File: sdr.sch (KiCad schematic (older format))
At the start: 3 parts

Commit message: RF filter implemented
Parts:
- U?: symbol RF_Mixer:ADE-6 -> sdr-rescue:ADE-6-RF_Mixer
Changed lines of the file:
@@
 S 1500 3350 750  250
 U 5FE31D05
-F0 "Sheet5FE31D04" 50
+F0 "30MHz LPF" 50
 F1 "rf_lpf.sch" 50
 F2 "IN" I L 1500 3450 50
-F3 "OUT" I R 2250 3450 50
+F3 "OUT" O R 2250 3450 50
 $EndSheet
 $Sheet
@@
 $EndSheet
 $Comp
-L RF_Mixer:ADE-6 U?
+L sdr-rescue:ADE-6-RF_Mixer U?
 U 1 1 5FE32B05
 P 4100 3450

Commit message: Attenuator revised
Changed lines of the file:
@@
 F3 "OUT" O R 2250 3450 50
-$EndSheet
-$Sheet
-S 2600 3350 900  250
-U 5FE31E1E
-F0 "Sheet5FE31E1D" 50
-F1 "rf_autt.sch" 50
 $EndSheet
 $Comp
@@
 	1    0    0    -1
 $EndComp
+$Sheet
+S 2600 3350 900  600
+U 5FE31E1E
+F0 "Attenuator" 50
+F1 "rf_autt.sch" 50
+F2 "IN" I L 2600 3450 50
+F3 "OUT" O R 3500 3450 50
+F4 "ATT_SEL0" I L 2600 3750 50
+F5 "ATT_SEL1" I L 2600 3850 50
+$EndSheet
+Wire Wire Line
+	2250 3450 2600 3450
 $EndSCHEMATC

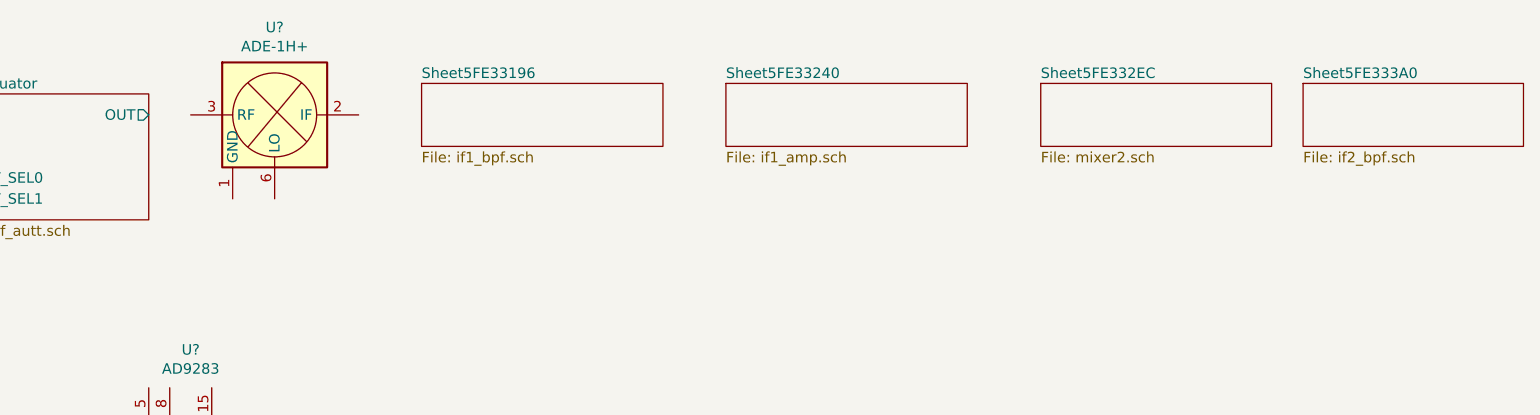
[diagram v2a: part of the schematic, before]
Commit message: Second mixer
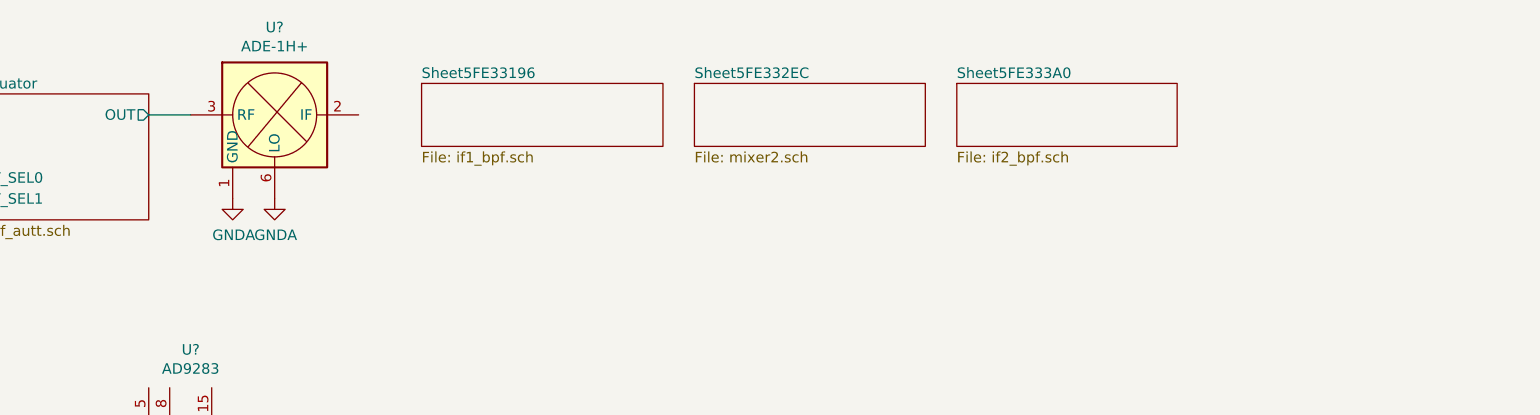
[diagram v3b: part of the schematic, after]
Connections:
- net Attenuator/OUT: now also U?.3 (RF)
- net GNDA: now also U?.1 (GND), U?.4 (GND), U?.5 (GND), U?.6 (LO)
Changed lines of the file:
@@
 $Descr A4 11693 8268
 encoding utf-8
-Sheet 1 8
+Sheet 1 7
 Title ""
 Date ""
@@
 $EndSheet
 $Sheet
-S 6250 3300 1150 300
-U 5FE33241
-F0 "Sheet5FE33240" 50
-F1 "if1_amp.sch" 50
-$EndSheet
-$Sheet
-S 7750 3300 1100 300
+S 6100 3300 1100 300
 U 5FE332ED
 F0 "Sheet5FE332EC" 50
@@
 $EndSheet
 $Sheet
-S 9000 3300 1050 300
+S 7350 3300 1050 300
 U 5FE333A1
 F0 "Sheet5FE333A0" 50
@@
 Wire Wire Line
 	2250 3450 2600 3450
+Wire Wire Line
+	3500 3450 3700 3450
+$Comp
+L power:GNDA #PWR?
+U 1 1 5FE67095
+P 3900 3850
+F 0 "#PWR?" H 3900 3600 50  0001 C CNN
+F 1 "GNDA" H 3905 3677 50  0000 C CNN
+F 2 "" H 3900 3850 50  0001 C CNN
+F 3 "" H 3900 3850 50  0001 C CNN
+	1    3900 3850
+	1    0    0    -1
+$EndComp
+$Comp
+L power:GNDA #PWR?
+U 1 1 5FE6714C
+P 4100 3850
+F 0 "#PWR?" H 4100 3600 50  0001 C CNN
+F 1 "GNDA" H 4105 3677 50  0000 C CNN
+F 2 "" H 4100 3850 50  0001 C CNN
+F 3 "" H 4100 3850 50  0001 C CNN
+	1    4100 3850
+	1    0    0    -1
+$EndComp
 $EndSCHEMATC

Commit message: 37.4Mega
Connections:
- net 37.4 MHz Butterworth BPF/IN: now reaches U?.2 (IF)
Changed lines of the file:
@@
 S 4800 3300 1150 300
 U 5FE33197
-F0 "Sheet5FE33196" 50
+F0 "37.4 MHz Butterworth BPF" 50
 F1 "if1_bpf.sch" 50
+F2 "IN" I L 4800 3450 50
+F3 "OUT" I R 5950 3450 50
 $EndSheet
 $Sheet
@@
 	1    0    0    -1
 $EndComp
+Wire Wire Line
+	4800 3450 4500 3450
 $EndSCHEMATC

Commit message: Block diagram arrangement
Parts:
- added K? (x3): FRT5_separated, Relay_THT:Relay_DPDT_FRT5, symbol Relay:FRT5_separated
- added R?: 0 DNP, symbol Device:R
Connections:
- wire segments 4 -> 23
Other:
- note added: "Switchable bga2866??"
- moved on the sheet: J?, U?
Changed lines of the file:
@@
 L Connector:Conn_Coaxial J?
 U 1 1 5FE31A99
-P 850 3450
-F 0 "J?" H 778 3688 50  0000 C CNN
-F 1 "Conn_Coaxial" H 778 3597 50  0000 C CNN
-F 2 "" H 850 3450 50  0001 C CNN
-F 3 " ~" H 850 3450 50  0001 C CNN
-	1    850  3450
+P 850 3650
+F 0 "J?" H 778 3888 50  0000 C CNN
+F 1 "Conn_Coaxial" H 778 3797 50  0000 C CNN
+F 2 "" H 850 3650 50  0001 C CNN
+F 3 " ~" H 850 3650 50  0001 C CNN
+	1    850  3650
 	-1   0    0    -1
 $EndComp
 $Sheet
-S 1500 3350 750  250
+S 1150 1250 750  250
 U 5FE31D05
 F0 "30MHz LPF" 50
 F1 "rf_lpf.sch" 50
-F2 "IN" I L 1500 3450 50
-F3 "OUT" O R 2250 3450 50
+F2 "IN" I L 1150 1350 50
+F3 "OUT" O R 1900 1350 50
 $EndSheet
 $Comp
 L sdr-rescue:ADE-6-RF_Mixer U?
 U 1 1 5FE32B05
-P 4100 3450
-F 0 "U?" H 4100 3867 50  0000 C CNN
-F 1 "ADE-1H+" H 4100 3776 50  0000 C CNN
-F 2 "RF_Mini-Circuits:Mini-Circuits_CD542_LandPatternPL-052" H 4175 3075 50  0001 C CNN
-F 3 "https://www.minicircuits.com/pdfs/ADE-6.pdf" H 4275 3175 50  0001 C CNN
-	1    4100 3450
+P 3300 1350
+F 0 "U?" H 3300 1767 50  0000 C CNN
+F 1 "ADE-1H+" H 3300 1676 50  0000 C CNN
+F 2 "RF_Mini-Circuits:Mini-Circuits_CD542_LandPatternPL-052" H 3375 975 50  0001 C CNN
+F 3 "https://www.minicircuits.com/pdfs/ADE-6.pdf" H 3475 1075 50  0001 C CNN
+	1    3300 1350
 	1    0    0    -1
 $EndComp
 $Sheet
-S 4800 3300 1150 300
+S 3750 1200 1250 300
 U 5FE33197
 F0 "37.4 MHz Butterworth BPF" 50
 F1 "if1_bpf.sch" 50
-F2 "IN" I L 4800 3450 50
-F3 "OUT" I R 5950 3450 50
+F2 "IN" I L 3750 1350 50
+F3 "OUT" I R 5000 1350 50
 $EndSheet
 $Sheet
-S 6100 3300 1100 300
+S 5100 1200 1450 300
 U 5FE332ED
-F0 "Sheet5FE332EC" 50
+F0 "37.4 MHz Amp, and 2nd mixer" 50
 F1 "mixer2.sch" 50
+F2 "out_p" I R 6550 1300 50
+F3 "out_n" I R 6550 1400 50
+F4 "IN" I L 5100 1350 50
 $EndSheet
 $Sheet
-S 7350 3300 1050 300
+S 6700 1200 1050 300
 U 5FE333A1
 F0 "Sheet5FE333A0" 50
@@
 $EndSheet
 $Sheet
-S 750  5050 1300 350
+S 7850 1200 1300 350
 U 5FE3342F
 F0 "Sheet5FE3342E" 50
@@
 L Analog_ADC:AD9283 U?
 U 1 1 5FE337CA
-P 3700 5550
-F 0 "U?" H 3700 6531 50  0000 C CNN
-F 1 "AD9283" H 3700 6440 50  0000 C CNN
-F 2 "" H 3700 5550 50  0001 C CNN
-F 3 "https://www.analog.com/media/en/technical-documentation/data-sheets/AD9283.pdf" H 3700 5550 50  0001 C CNN
-	1    3700 5550
-	1    0    0    -1
-$EndComp
-Wire Wire Line
-	1500 3450 1050 3450
-$Comp
-L power:GNDA #PWR?
-U 1 1 5FE34F57
-P 850 3650
-F 0 "#PWR?" H 850 3400 50  0001 C CNN
-F 1 "GNDA" H 855 3477 50  0000 C CNN
-F 2 "" H 850 3650 50  0001 C CNN
-F 3 "" H 850 3650 50  0001 C CNN
-	1    850  3650
-	1    0    0    -1
-$EndComp
-$Sheet
-S 2600 3350 900  600
-U 5FE31E1E
-F0 "Attenuator" 50
-F1 "rf_autt.sch" 50
-F2 "IN" I L 2600 3450 50
-F3 "OUT" O R 3500 3450 50
-F4 "ATT_SEL0" I L 2600 3750 50
-F5 "ATT_SEL1" I L 2600 3850 50
-$EndSheet
-Wire Wire Line
-	2250 3450 2600 3450
-Wire Wire Line
-	3500 3450 3700 3450
-$Comp
-L power:GNDA #PWR?
-U 1 1 5FE67095
-P 3900 3850
-F 0 "#PWR?" H 3900 3600 50  0001 C CNN
-F 1 "GNDA" H 3905 3677 50  0000 C CNN
-F 2 "" H 3900 3850 50  0001 C CNN
-F 3 "" H 3900 3850 50  0001 C CNN
-	1    3900 3850
+P 10050 1700
+F 0 "U?" H 10050 2681 50  0000 C CNN
+F 1 "AD9283" H 10050 2590 50  0000 C CNN
+F 2 "" H 10050 1700 50  0001 C CNN
+F 3 "https://www.analog.com/media/en/technical-documentation/data-sheets/AD9283.pdf" H 10050 1700 50  0001 C CNN
+	1    10050 1700
 	1    0    0    -1
 $EndComp
 $Comp
 L power:GNDA #PWR?
-U 1 1 5FE6714C
-P 4100 3850
-F 0 "#PWR?" H 4100 3600 50  0001 C CNN
-F 1 "GNDA" H 4105 3677 50  0000 C CNN
-F 2 "" H 4100 3850 50  0001 C CNN
-F 3 "" H 4100 3850 50  0001 C CNN
-	1    4100 3850
+U 1 1 5FE34F57
+P 850 3850
+F 0 "#PWR?" H 850 3600 50  0001 C CNN
+F 1 "GNDA" H 855 3677 50  0000 C CNN
+F 2 "" H 850 3850 50  0001 C CNN
+F 3 "" H 850 3850 50  0001 C CNN
+	1    850  3850
+	1    0    0    -1
+$EndComp
+$Sheet
+S 2050 1250 700  600
+U 5FE31E1E
+F0 "Attenuator" 50
+F1 "rf_autt.sch" 50
+F2 "IN" I L 2050 1350 50
+F3 "OUT" O R 2750 1350 50
+F4 "ATT_SEL0" I L 2050 1650 50
+F5 "ATT_SEL1" I L 2050 1750 50
+$EndSheet
+Wire Wire Line
+	1900 1350 1950 1350
+$Comp
+L power:GNDA #PWR?
+U 1 1 5FE67095
+P 3100 1750
+F 0 "#PWR?" H 3100 1500 50  0001 C CNN
+F 1 "GNDA" H 3105 1577 50  0000 C CNN
+F 2 "" H 3100 1750 50  0001 C CNN
+F 3 "" H 3100 1750 50  0001 C CNN
+	1    3100 1750
 	1    0    0    -1
 $EndComp
 Wire Wire Line
-	4800 3450 4500 3450
+	3750 1350 3700 1350
+$Comp
+L Device:R R?
+U 1 1 5FE74C58
+P 2450 1000
+F 0 "R?" V 2243 1000 50  0000 C CNN
+F 1 "0 DNP" V 2334 1000 50  0000 C CNN
+F 2 "" V 2380 1000 50  0001 C CNN
+F 3 "~" H 2450 1000 50  0001 C CNN
+	1    2450 1000
+	0    1    1    0
+$EndComp
+Wire Wire Line
+	2850 1350 2850 1000
+Wire Wire Line
+	2850 1000 2600 1000
+Connection ~ 2850 1350
+Wire Wire Line
+	2850 1350 2900 1350
+Wire Wire Line
+	2300 1000 1950 1000
+Wire Wire Line
+	1950 1000 1950 1350
+Connection ~ 1950 1350
+Wire Wire Line
+	1950 1350 2050 1350
+Wire Wire Line
+	2750 1350 2850 1350
+Wire Wire Line
+	5100 1350 5000 1350
+$Comp
+L Relay:FRT5_separated K?
+U 1 1 5FE86F08
+P 1400 6450
+F 0 "K?" H 1555 6496 50  0000 L CNN
+F 1 "FRT5_separated" H 1555 6405 50  0000 L CNN
+F 2 "Relay_THT:Relay_DPDT_FRT5" H 1600 6350 50  0001 L CNN
+F 3 "https://www.elpro.org/de/index.php?controller=attachment&id_attachment=8663" H 1400 6450 50  0001 C CNN
+	1    1400 6450
+	1    0    0    -1
+$EndComp
+$Comp
+L Relay:FRT5_separated K?
+U 2 1 5FE88F75
+P 1500 3650
+F 0 "K?" V 1175 3650 50  0000 C CNN
+F 1 "FRT5_separated" V 1266 3650 50  0000 C CNN
+F 2 "Relay_THT:Relay_DPDT_FRT5" H 1700 3550 50  0001 L CNN
+F 3 "https://www.elpro.org/de/index.php?controller=attachment&id_attachment=8663" H 1500 3650 50  0001 C CNN
+	2    1500 3650
+	0    1    1    0
+$EndComp
+$Comp
+L Relay:FRT5_separated K?
+U 3 1 5FE89BA9
+P 2200 4100
+F 0 "K?" H 2344 4146 50  0000 L CNN
+F 1 "FRT5_separated" H 2344 4055 50  0000 L CNN
+F 2 "Relay_THT:Relay_DPDT_FRT5" H 2400 4000 50  0001 L CNN
+F 3 "https://www.elpro.org/de/index.php?controller=attachment&id_attachment=8663" H 2200 4100 50  0001 C CNN
+	3    2200 4100
+	1    0    0    -1
+$EndComp
+Wire Wire Line
+	1800 3550 1900 3550
+Wire Wire Line
+	1900 3550 1900 2100
+Wire Wire Line
+	1900 2100 800  2100
+Wire Wire Line
+	800  2100 800  1350
+Wire Wire Line
+	800  1350 1150 1350
+Wire Wire Line
+	1200 3650 1050 3650
+Wire Wire Line
+	2100 3800 2100 3750
+Wire Wire Line
+	2100 3750 1800 3750
+Wire Wire Line
+	2300 3800 2300 2100
+Wire Wire Line
+	2300 2100 3300 2100
+Wire Wire Line
+	3300 2100 3300 1750
+Wire Wire Line
+	2200 4400 10750 4400
+Wire Wire Line
+	10750 4400 10750 5100
+Text Notes 6250 1850 0    50   ~ 0
+Switchable bga2866??
 $EndSCHEMATC

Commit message: 2nd IF amp test values
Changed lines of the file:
@@
 Wire Wire Line
 	10750 4400 10750 5100
-Text Notes 6250 1850 0    50   ~ 0
+Text Notes 4650 1800 0    50   ~ 0
 Switchable bga2866??
 $EndSCHEMATC

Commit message: if2_amp.sch
if2_amp almost done
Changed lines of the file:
@@
 F0 "Sheet5FE3342E" 50
 F1 "if2_amp.sch" 50
+F2 "In+" I L 7850 1300 50
+F3 "In-" I L 7850 1450 50
+F4 "Out+" I R 9150 1300 50
+F5 "Out-" I R 9150 1450 50
 $EndSheet
 $Comp

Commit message: if2 completed
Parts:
- added R? (x2): 0 DNP, symbol Device:R
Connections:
- wire segments 23 -> 41
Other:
- moved on the sheet: U?
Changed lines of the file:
@@
 $EndSheet
 $Sheet
-S 6700 1200 1050 300
+S 6700 1200 950  400
 U 5FE333A1
 F0 "Sheet5FE333A0" 50
 F1 "if2_bpf.sch" 50
+F2 "Out+" I R 7650 1300 50
+F3 "Out-" I R 7650 1500 50
+F4 "In+" I L 6700 1300 50
+F5 "In-" I L 6700 1400 50
 $EndSheet
 $Sheet
-S 7850 1200 1300 350
+S 7850 1100 1300 500
 U 5FE3342F
 F0 "Sheet5FE3342E" 50
 F1 "if2_amp.sch" 50
 F2 "In+" I L 7850 1300 50
-F3 "In-" I L 7850 1450 50
+F3 "In-" I L 7850 1500 50
 F4 "Out+" I R 9150 1300 50
-F5 "Out-" I R 9150 1450 50
+F5 "Out-" I R 9150 1500 50
 $EndSheet
 $Comp
 L Analog_ADC:AD9283 U?
 U 1 1 5FE337CA
-P 10050 1700
-F 0 "U?" H 10050 2681 50  0000 C CNN
-F 1 "AD9283" H 10050 2590 50  0000 C CNN
-F 2 "" H 10050 1700 50  0001 C CNN
-F 3 "https://www.analog.com/media/en/technical-documentation/data-sheets/AD9283.pdf" H 10050 1700 50  0001 C CNN
-	1    10050 1700
+P 10100 1700
+F 0 "U?" H 10100 2681 50  0000 C CNN
+F 1 "AD9283" H 10100 2590 50  0000 C CNN
+F 2 "" H 10100 1700 50  0001 C CNN
+F 3 "https://www.analog.com/media/en/technical-documentation/data-sheets/AD9283.pdf" H 10100 1700 50  0001 C CNN
+	1    10100 1700
 	1    0    0    -1
 $EndComp
@@
 Text Notes 4650 1800 0    50   ~ 0
 Switchable bga2866??
+$Comp
+L Device:R R?
+U 1 1 5FEA317B
+P 8500 850
+F 0 "R?" V 8293 850 50  0000 C CNN
+F 1 "0 DNP" V 8384 850 50  0000 C CNN
+F 2 "" V 8430 850 50  0001 C CNN
+F 3 "~" H 8500 850 50  0001 C CNN
+	1    8500 850
+	0    1    1    0
+$EndComp
+$Comp
+L Device:R R?
+U 1 1 5FEA3DAB
+P 8500 2000
+F 0 "R?" V 8293 2000 50  0000 C CNN
+F 1 "0 DNP" V 8384 2000 50  0000 C CNN
+F 2 "" V 8430 2000 50  0001 C CNN
+F 3 "~" H 8500 2000 50  0001 C CNN
+	1    8500 2000
+	0    1    1    0
+$EndComp
+Wire Wire Line
+	7850 1300 7800 1300
+Wire Wire Line
+	7800 1300 7800 850
+Wire Wire Line
+	7800 850  8350 850
+Wire Wire Line
+	8650 850  9300 850
+Wire Wire Line
+	9300 850  9300 1300
+Wire Wire Line
+	9150 1300 9300 1300
+Wire Wire Line
+	9300 1500 9150 1500
+Wire Wire Line
+	9400 1500 9300 1500
+Connection ~ 9300 1500
+Wire Wire Line
+	9400 1300 9300 1300
+Connection ~ 9300 1300
+Wire Wire Line
+	9300 2000 8650 2000
+Wire Wire Line
+	9300 1500 9300 2000
+Wire Wire Line
+	7800 1500 7800 2000
+Wire Wire Line
+	7800 2000 8350 2000
+Wire Wire Line
+	7650 1300 7800 1300
+Connection ~ 7800 1300
+Wire Wire Line
+	7600 1500 7800 1500
+Connection ~ 7800 1500
+Wire Wire Line
+	7800 1500 7850 1500
+Wire Wire Line
+	6700 1300 6550 1300
+Wire Wire Line
+	6550 1400 6700 1400
 $EndSCHEMATC
